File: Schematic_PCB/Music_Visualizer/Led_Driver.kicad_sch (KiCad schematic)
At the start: 91 parts, among them U10 LM3915N-1, U11 LM3915N-1, U12 LM3915N-1, U13 LM3915N-1, U14 LM3915N-1, U15 LM3915N-1, U16 LM3915N-1

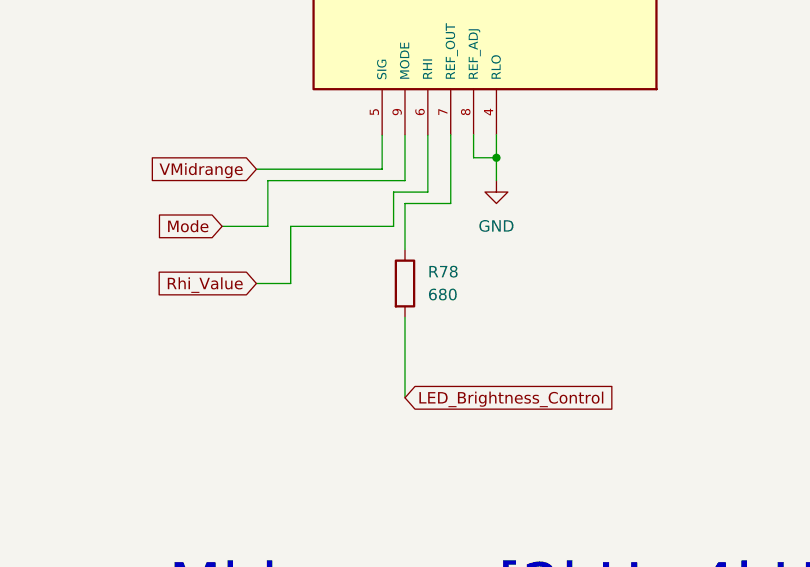
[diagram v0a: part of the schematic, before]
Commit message: Remove jacks and compact placement
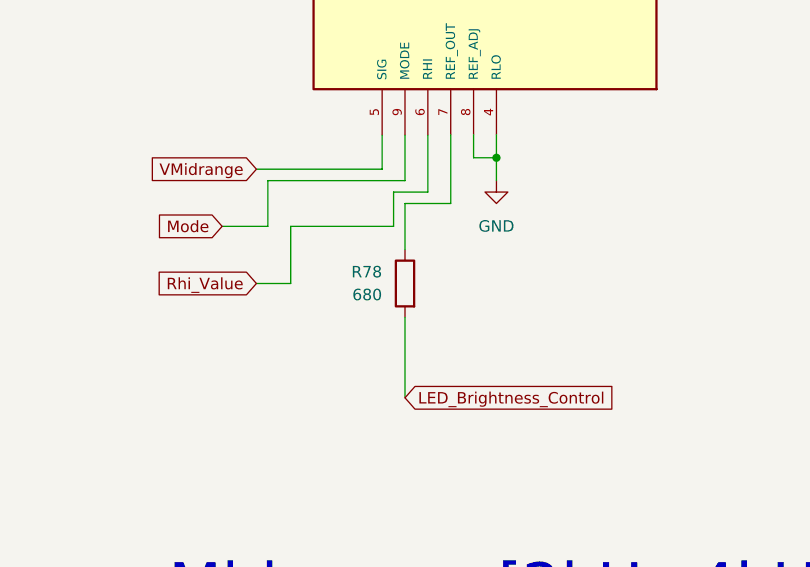
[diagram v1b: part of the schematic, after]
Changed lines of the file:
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@@
 		(lib_id "Device:R")
 		(at 80.01 254 0)
+		(mirror y)
 		(unit 1)
 		(exclude_from_sim no)
@@
 		(on_board yes)
 		(dnp no)
-		(fields_autoplaced yes)
 		(property "Reference" "R78"
-			(at 82.55 252.7299 0)
+			(at 77.47 252.7299 0)
 			(effects
 				(font
@@
 		)
 		(property "Value" "680"
-			(at 82.55 255.2699 0)
+			(at 77.47 255.2699 0)
 			(effects
 				(font
@@
 		)
 		(property "Footprint" "Custom_Footprints:R_0805_2012Metric_Pad1.20x1.40mm_HandSolder"
-			(at 78.232 254 90)
+			(at 81.788 254 90)
 			(effects
 				(font

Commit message: pre RDC
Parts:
- C56: footprint Custom_Footprints:C_0805_2012Metric_Pad1.18x1.45mm_HandSolder -> Custom_Footprints:custom_C_0805_2012Metric_Pad1.18x1.45mm_HandSolder
- C57: footprint Capacitor_THT:CP_Radial_D5.0mm_P2.00mm -> Capacitor_SMD:CP_Elec_4x5.4
- D1, D11, D12, D13, D14, D15, D16, D17, D2, D21, D22, D23, D24, D25, D26, D27, D3, D31, D32, D33, D34, D35, D36, D37, D4, D41, D42, D43, D44, D45, D46, D47, D5, D51, D52, D53, D54, D55, D56, D57, D6, D61, D62, D63, D64, D65, D66, D67, D7: footprint LED_SMD:LED_1210_3225Metric_Pad1.42x2.65mm_HandSolder -> PCM_SparkFun-LED:LED_1206_3216Metric_Green
- D10, D20, D30, D40, D50, D60, D70: footprint LED_SMD:LED_1210_3225Metric_Pad1.42x2.65mm_HandSolder -> PCM_SparkFun-LED:LED_1206_3216Metric_Red
- D18, D19, D28, D29, D38, D39, D48, D49, D58, D59, D68, D69, D8, D9: footprint LED_SMD:LED_1210_3225Metric_Pad1.42x2.65mm_HandSolder -> PCM_SparkFun-LED:LED_1206_3216Metric_Yellow
- T_ref1: renamed from TP12; footprint Custom_Footprints:TEST1Y -> Custom_Footprints:NEW_2_TestPoint_Loop_D2.60mm_Drill0.9mm_Beaded
- U10, U11, U12, U13, U14, U15, U16: footprint Package_DIP:DIP-18_W7.62mm_Socket -> Package_DIP:DIP-18_W7.62mm
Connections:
- net GND: now also RV1.3; no longer RV1.1
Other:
- moved on the sheet: RV1

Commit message: backup
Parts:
- removed JP2: Jumper_2_Open, Connector_PinHeader_2.54mm:PinHeader_2x01_P2.54mm_Vertical, symbol Jumper:Jumper_2_Open
- added SW3: SW_SPST, Button_Switch_THT:SW_Slide-03_Wuerth-WS-SLTV_10x2.5x6.4_P2.54mm, symbol Switch:SW_Nidec_CAS-120A1
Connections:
- net +9V: now also SW3.1 (C)
- net GND: now also SW3.3 (A)
- net Mode: now also SW3.2 (B)
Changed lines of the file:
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@@
 	(wire
 		(pts
-			(xy 227.33 209.55) (xy 237.49 209.55)
+			(xy 227.33 207.01) (xy 237.49 207.01)
 		)
 		(stroke
@@
 	)
 	(symbol
+		(lib_id "Switch:SW_Nidec_CAS-120A1")
+		(at 242.57 209.55 180)
+		(unit 1)
+		(body_style 1)
+		(exclude_from_sim no)
+		(in_bom yes)
+		(on_board yes)
+		(in_pos_files yes)
+		(dnp no)
+		(fields_autoplaced yes)
+		(property "Reference" "SW3"
+			(at 242.57 200.66 0)
+			(show_name no)
+			(do_not_autoplace no)
+			(effects
+				(font
+					(size 1.27 1.27)
+				)
+			)
+		)
+		(property "Value" "SW_SPST"
+			(at 242.57 203.2 0)
+			(show_name no)
+			(do_not_autoplace no)
+			(effects
+				(font
+					(size 1.27 1.27)
+				)
+			)
+		)
+		(property "Footprint" "Button_Switch_THT:SW_Slide-03_Wuerth-WS-SLTV_10x2.5x6.4_P2.54mm"
+			(at 242.57 199.39 0)
+			(hide yes)
+			(show_name no)
+			(do_not_autoplace no)
+			(effects
+				(font
+					(size 1.27 1.27)
+				)
+			)
+		)
+		(property "Datasheet" "https://www.nidec-components.com/e/catalog/switch/cas.pdf"
+			(at 242.57 201.93 0)
+			(hide yes)
+			(show_name no)
+			(do_not_autoplace no)
+			(effects
+				(font
+					(size 1.27 1.27)
+				)
+			)
+		)
+		(property "Description" "Switch, single pole double throw"
+			(at 242.57 209.55 0)
+			(hide yes)
+			(show_name no)
+			(do_not_autoplace no)
+			(effects
+				(font
+					(size 1.27 1.27)
+				)
+			)
+		)
+		(property "STANDART" ""
+			(at 242.57 209.55 0)
+			(hide yes)
+			(show_name no)
+			(do_not_autoplace no)
+			(effects
+				(font
+					(size 1.27 1.27)
+				)
+			)
+		)
+		(pin "1"
+		)
+		(pin "2"
+		)
+		(pin "3"
+		)
+		(instances
+			(project "Music_Visualizer"
+				(path "/236ff8a0-79ed-4eaf-ae36-90444797fa8d/56ed3a67-eed8-4688-8767-d6bf63bd87ca"
+					(reference "SW3")
+					(unit 1)
+				)
+			)
+		)
+	)
+	(symbol
 		(lib_id "Device:R")
 		(at 80.01 254 0)
@@
 	(symbol
 		(lib_id "power:+9V")
-		(at 227.33 209.55 0)
+		(at 227.33 207.01 0)
 		(unit 1)
 		(body_style 1)
@@
 		(fields_autoplaced yes)
 		(property "Reference" "#PWR082"
-			(at 227.33 213.36 0)
+			(at 227.33 210.82 0)
 			(hide yes)
 			(show_name no)
@@
 		)
 		(property "Value" "+9V"
-			(at 227.33 204.47 0)
+			(at 227.33 201.93 0)
 			(show_name no)
 			(do_not_autoplace no)
@@
 		)
 		(property "Footprint" ""
-			(at 227.33 209.55 0)
+			(at 227.33 207.01 0)
 			(hide yes)
 			(show_name no)
@@
 		)
 		(property "Datasheet" ""
-			(at 227.33 209.55 0)
+			(at 227.33 207.01 0)
 			(hide yes)
 			(show_name no)
@@
 		)
 		(property "Description" ""
-			(at 227.33 209.55 0)
+			(at 227.33 207.01 0)
 			(show_name no)
 			(do_not_autoplace no)
@@
 	)
 	(symbol
-		(lib_id "Jumper:Jumper_2_Open")
-		(at 242.57 209.55 0)
-		(unit 1)
-		(body_style 1)
-		(exclude_from_sim no)
-		(in_bom yes)
-		(on_board yes)
-		(in_pos_files yes)
-		(dnp no)
-		(fields_autoplaced yes)
-		(property "Reference" "JP2"
-			(at 242.57 203.2 0)
-			(show_name no)
-			(do_not_autoplace no)
-			(effects
-				(font
-					(size 1.27 1.27)
-				)
-			)
-		)
-		(property "Value" "Jumper_2_Open"
-			(at 242.57 205.74 0)
-			(show_name no)
-			(do_not_autoplace no)
-			(effects
-				(font
-					(size 1.27 1.27)
-				)
-			)
-		)
-		(property "Footprint" "Connector_PinHeader_2.54mm:PinHeader_2x01_P2.54mm_Vertical"
-			(at 242.57 209.55 0)
-			(hide yes)
-			(show_name no)
-			(do_not_autoplace no)
-			(effects
-				(font
-					(size 1.27 1.27)
-				)
-			)
-		)
-		(property "Datasheet" "https://www.mouser.ca/datasheet/2/181/M20-999-1218971.pdf"
-			(at 242.57 209.55 0)
-			(hide yes)
-			(show_name no)
-			(do_not_autoplace no)
-			(effects
-				(font
-					(size 1.27 1.27)
-				)
-			)
-		)
-		(property "Description" ""
-			(at 242.57 209.55 0)
-			(show_name no)
-			(do_not_autoplace no)
-			(effects
-				(font
-					(size 1.27 1.27)
-				)
-			)
-		)
-		(property "STANDART" ""
-			(at 242.57 209.55 0)
-			(hide yes)
-			(show_name no)
-			(do_not_autoplace no)
-			(effects
-				(font
-					(size 1.27 1.27)
-				)
-			)
-		)
-		(pin "1"
-		)
-		(pin "2"
-		)
-		(instances
-			(project "Music_Visualizer"
-				(path "/236ff8a0-79ed-4eaf-ae36-90444797fa8d/56ed3a67-eed8-4688-8767-d6bf63bd87ca"
-					(reference "JP2")
-					(unit 1)
-				)
-			)
-			(project "Led_Driver"
-				(path "/8d68b169-ddb7-43b3-887e-9471d5c44fe5"
-					(reference "JP?")
-					(unit 1)
-				)
-			)
-		)
-	)
-	(symbol
 		(lib_id "power:+9V")
 		(at 198.12 294.64 0)
@@
 					(unit 1)
 				)
+			)
+		)
+	)
+	(symbol
+		(lib_id "power:GND")
+		(at 237.49 212.09 0)
+		(unit 1)
+		(body_style 1)
+		(exclude_from_sim no)
+		(in_bom yes)
+		(on_board yes)
+		(in_pos_files yes)
+		(dnp no)
+		(fields_autoplaced yes)
+		(property "Reference" "#PWR043"
+			(at 237.49 218.44 0)
+			(hide yes)
+			(show_name no)
+			(do_not_autoplace no)
+			(effects
+				(font
+					(size 1.27 1.27)
+				)
+			)
+		)
+		(property "Value" "GND"
+			(at 237.49 217.17 0)
+			(show_name no)
+			(do_not_autoplace no)
+			(effects
+				(font
+					(size 1.27 1.27)
+				)
+			)
+		)
+		(property "Footprint" ""
+			(at 237.49 212.09 0)
+			(hide yes)
+			(show_name no)
+			(do_not_autoplace no)
+			(effects
+				(font
+					(size 1.27 1.27)
+				)
+			)
+		)
+		(property "Datasheet" ""
+			(at 237.49 212.09 0)
+			(hide yes)
+			(show_name no)
+			(do_not_autoplace no)
+			(effects
+				(font
+					(size 1.27 1.27)
+				)
+			)
+		)
+		(property "Description" ""
+			(at 237.49 212.09 0)
+			(show_name no)
+			(do_not_autoplace no)
+			(effects
+				(font
+					(size 1.27 1.27)
+				)
+			)
+		)
+		(pin "1"
+		)
+		(instances
+			(project "Music_Visualizer"
+				(path "/236ff8a0-79ed-4eaf-ae36-90444797fa8d/56ed3a67-eed8-4688-8767-d6bf63bd87ca"
+					(reference "#PWR043")
+					(unit 1)
+				)
